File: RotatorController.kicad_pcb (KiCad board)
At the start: 2 copper layers, 99 x 70 mm, 58 parts, among them J1 USB_A, J2 Rotator, J4 Motor Cap, K1 G5LE-1, K2 G5LE-1, K3 G5LE-1, Q1 BSS123, Q2 BSS123, Q3 BSS123, SW1 CW, SW2 CCW, U1 Teensy4.0, U3 AP2161W

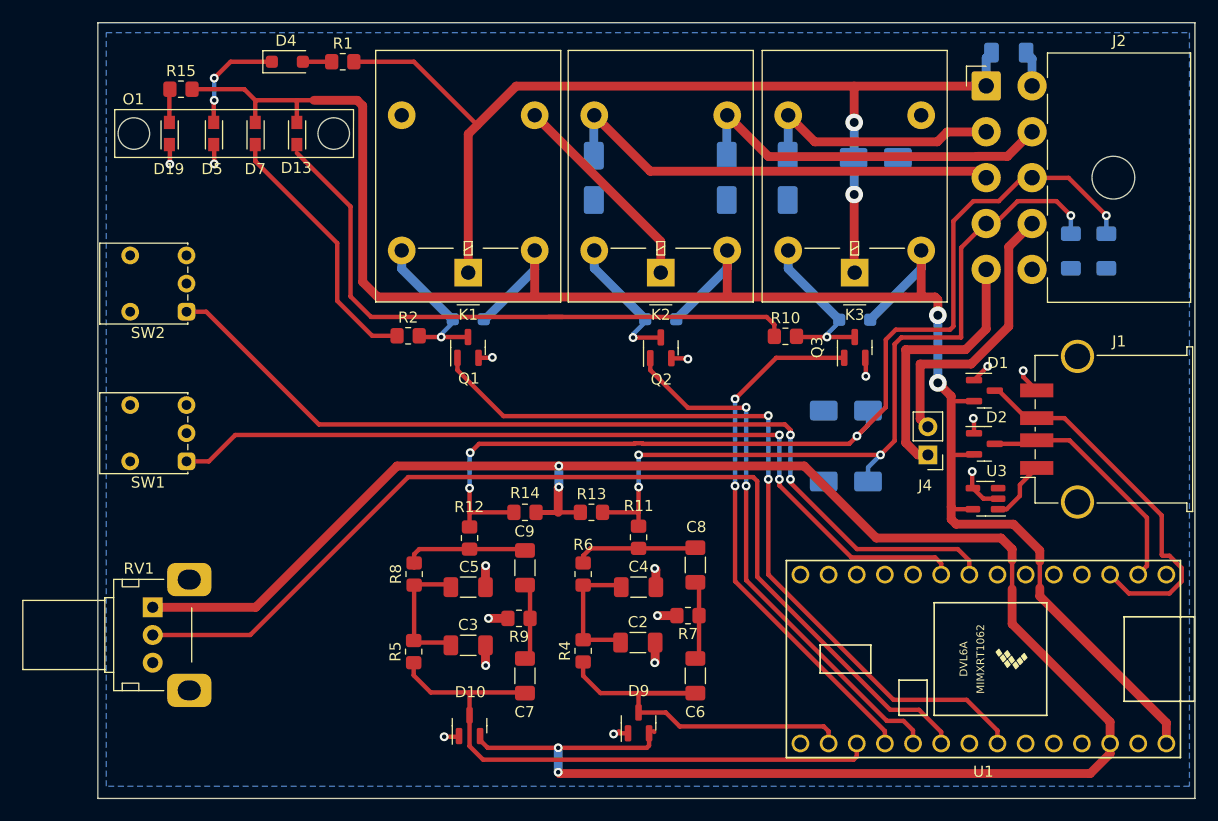
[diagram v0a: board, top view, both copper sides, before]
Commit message: Created V3 branch for new board with 3.6V zeners for protection
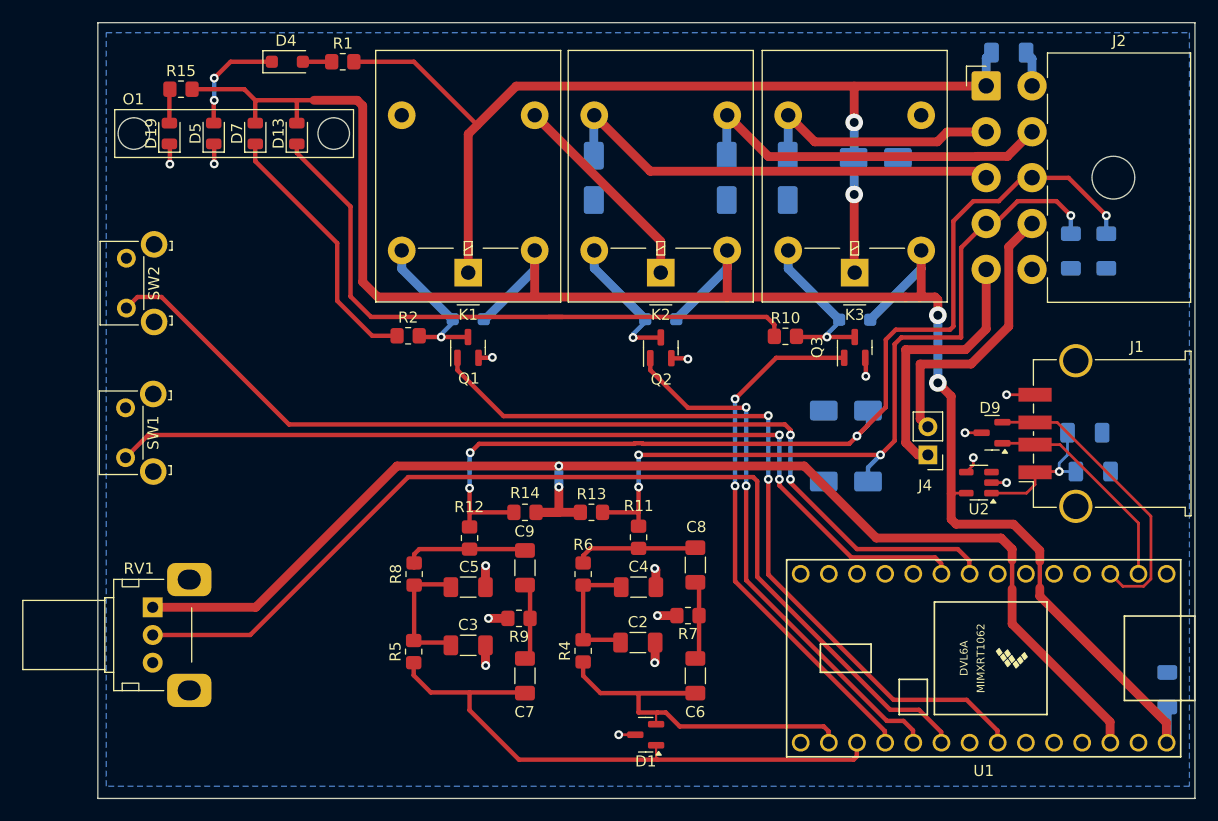
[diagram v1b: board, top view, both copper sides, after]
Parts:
- removed D10, D2: BAS40-04, Package_TO_SOT_SMD:SOT-23
- removed U3: AP2161W, Package_TO_SOT_SMD:SOT-23-5
- added C10: 0.1, Capacitor_SMD:C_1206_3216Metric_Pad1.33x1.80mm_HandSolder, B.Cu at (191.5, 115.2)
- added C13: 0.1, Capacitor_SMD:C_1206_3216Metric_Pad1.33x1.80mm_HandSolder, B.Cu at (184.8, 95.5)
- added C14: 120u, Capacitor_SMD:C_1206_3216Metric_Pad1.33x1.80mm_HandSolder, B.Cu at (184.1, 92.0)
- added U2: AP2161W, Package_TO_SOT_SMD:SOT-23-5, F.Cu at (174.5, 96.5)
- D1, D9: value BAS40-04 -> 2BZX84C3V6
- D13, D19, D7: footprint LED_SMD:LED_miniPLCC_2315_Handsoldering -> LED_SMD:LED_0805_2012Metric
- D5: value 26V -> 26VAC; footprint LED_SMD:LED_miniPLCC_2315_Handsoldering -> LED_SMD:LED_0805_2012Metric
- J1: value USB_A -> Serial
- SW1: footprint Button_Switch_THT:SW_Push_1P2T_Vertical_E-Switch_800UDP8P1A1M6 -> Button_Switch_THT:SW_SPST_Omron_B3F-315x_Angled
- SW2: value CCW -> CW; footprint Button_Switch_THT:SW_Push_1P2T_Vertical_E-Switch_800UDP8P1A1M6 -> Button_Switch_THT:SW_SPST_Omron_B3F-315x_Angled
- moved D1 43.6 mm to (144.4, 119.2), turned to 180 degrees
- moved D9 41.3 mm to (175.7, 92.0), turned to 180 degrees
- moved SW1 5.51 mm to (97.5, 94.2), turned to 90 degrees
- moved SW2 5.44 mm to (97.6, 80.8), turned to 90 degrees
- moved J1 0.42 mm to (185.9, 92.1)
- moved U1 0.07 mm to (174.9, 112.3)
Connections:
- D1 pad 1: GND -> /Flt_W-
- D1 pad 2: /+5V -> /Flt_W+
- D1 pad 3: /Ctlr_Tx -> GND
- D9 pad 1: GND -> /Ctlr_Rx
- D9 pad 2: /3V3 -> /Ctlr_Tx
- D9 pad 3: /Flt_W+ -> GND
- J1 pad 1: Net-(J1-VBUS) -> /5V_Serial
- RV1 pad MP: GND -> (no net)
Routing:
- net /3V3: track 188.2 -> 117.4 mm, vias 4 -> 2
- net /5V_Serial: track 0.00 -> 12.9 mm, vias 0 -> 1
- net /Ctlr_Tx: track 34.9 -> 27.0 mm
- net /CCW: track 84.0 -> 90.4 mm
- net /CW: track 77.3 -> 82.9 mm
- net Net-(J1-VBUS): track 5.61 -> 0.00 mm
- net GND: track 34.8 -> 30.2 mm, vias 17 -> 16
- net /Ctlr_Rx: track 22.2 -> 19.8 mm
- net /+5V: track 182.9 -> 181.7 mm
- net /Flt_W+: track 38.2 -> 39.3 mm
- net Net-(D13-K): track 56.6 -> 57.4 mm
- net /Flt_W-: track 53.4 -> 52.9 mm
